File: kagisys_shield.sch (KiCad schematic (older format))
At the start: 1 part, among them J1 Conn1

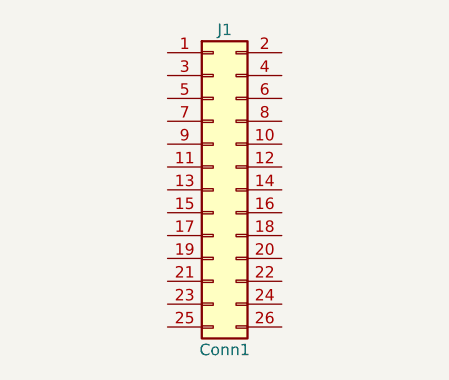
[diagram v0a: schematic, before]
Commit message: fix pin_layout
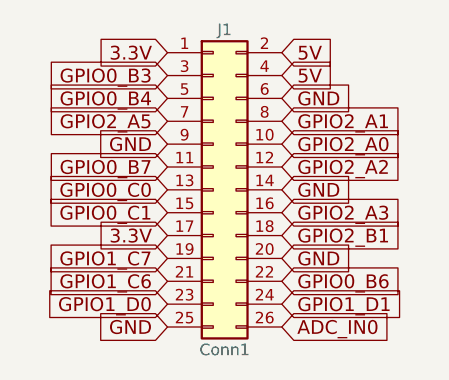
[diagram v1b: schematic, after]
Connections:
- net 3.3V: now reaches J1.1 (Pin_1)
- net 3.3V: now also J1.17 (Pin_17)
- net GPIO2_A0: now reaches J1.10 (Pin_10)
- net GPIO0_B7: now reaches J1.11 (Pin_11)
- net GPIO2_A2: now reaches J1.12 (Pin_12)
- net GPIO0_C0: now reaches J1.13 (Pin_13)
- net GND: now reaches J1.14 (Pin_14)
- net GND: now also J1.20 (Pin_20), J1.25 (Pin_25), J1.6 (Pin_6), J1.9 (Pin_9)
- net GPIO0_C1: now reaches J1.15 (Pin_15)
- net GPIO2_A3: now reaches J1.16 (Pin_16)
- net GPIO2_B1: now reaches J1.18 (Pin_18)
- net GPIO1_C7: now reaches J1.19 (Pin_19)
- net 5V: now reaches J1.2 (Pin_2)
- net 5V: now also J1.4 (Pin_4)
- net GPIO1_C6: now reaches J1.21 (Pin_21)
- net GPIO0_B6: now reaches J1.22 (Pin_22)
- net GPIO1_D0: now reaches J1.23 (Pin_23)
- net GPIO1_D1: now reaches J1.24 (Pin_24)
- net ADC_IN0: now reaches J1.26 (Pin_26)
- net GPIO0_B3: now reaches J1.3 (Pin_3)
- net GPIO0_B4: now reaches J1.5 (Pin_5)
- net GPIO2_A5: now reaches J1.7 (Pin_7)
- net GPIO2_A1: now reaches J1.8 (Pin_8)
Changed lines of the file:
@@
 	1    0    0    -1
 $EndComp
+Text GLabel 1350 1150 0    60   Input ~ 0
+3.3V
+Text GLabel 1850 1150 2    60   Input ~ 0
+5V
+Text GLabel 1850 1250 2    60   Input ~ 0
+5V
+Text GLabel 1850 1350 2    60   Input ~ 0
+GND
+Text GLabel 1350 1550 0    60   Input ~ 0
+GND
+Text GLabel 1350 1250 0    60   Input ~ 0
+GPIO0_B3
+Text GLabel 1350 1350 0    60   Input ~ 0
+GPIO0_B4
+Text GLabel 1350 1450 0    60   Input ~ 0
+GPIO2_A5
+Text GLabel 1350 1650 0    60   Input ~ 0
+GPIO0_B7
+Text GLabel 1350 1750 0    60   Input ~ 0
+GPIO0_C0
+Text GLabel 1350 1850 0    60   Input ~ 0
+GPIO0_C1
+Text GLabel 1350 1950 0    60   Input ~ 0
+3.3V
+Text GLabel 1350 2050 0    60   Input ~ 0
+GPIO1_C7
+Text GLabel 1350 2150 0    60   Input ~ 0
+GPIO1_C6
+Text GLabel 1350 2250 0    60   Input ~ 0
+GPIO1_D0
+Text GLabel 1350 2350 0    60   Input ~ 0
+GND
+Text GLabel 1850 1450 2    60   Input ~ 0
+GPIO2_A1
+Text GLabel 1850 1550 2    60   Input ~ 0
+GPIO2_A0
+Text GLabel 1850 1650 2    60   Input ~ 0
+GPIO2_A2
+Text GLabel 1850 1750 2    60   Input ~ 0
+GND
+Text GLabel 1850 1850 2    60   Input ~ 0
+GPIO2_A3
+Text GLabel 1850 1950 2    60   Input ~ 0
+GPIO2_B1
+Text GLabel 1850 2050 2    60   Input ~ 0
+GND
+Text GLabel 1850 2150 2    60   Input ~ 0
+GPIO0_B6
+Text GLabel 1850 2250 2    60   Input ~ 0
+GPIO1_D1
+Text GLabel 1850 2350 2    60   Input ~ 0
+ADC_IN0
 $EndSCHEMATC
